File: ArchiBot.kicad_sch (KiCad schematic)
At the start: 0 parts

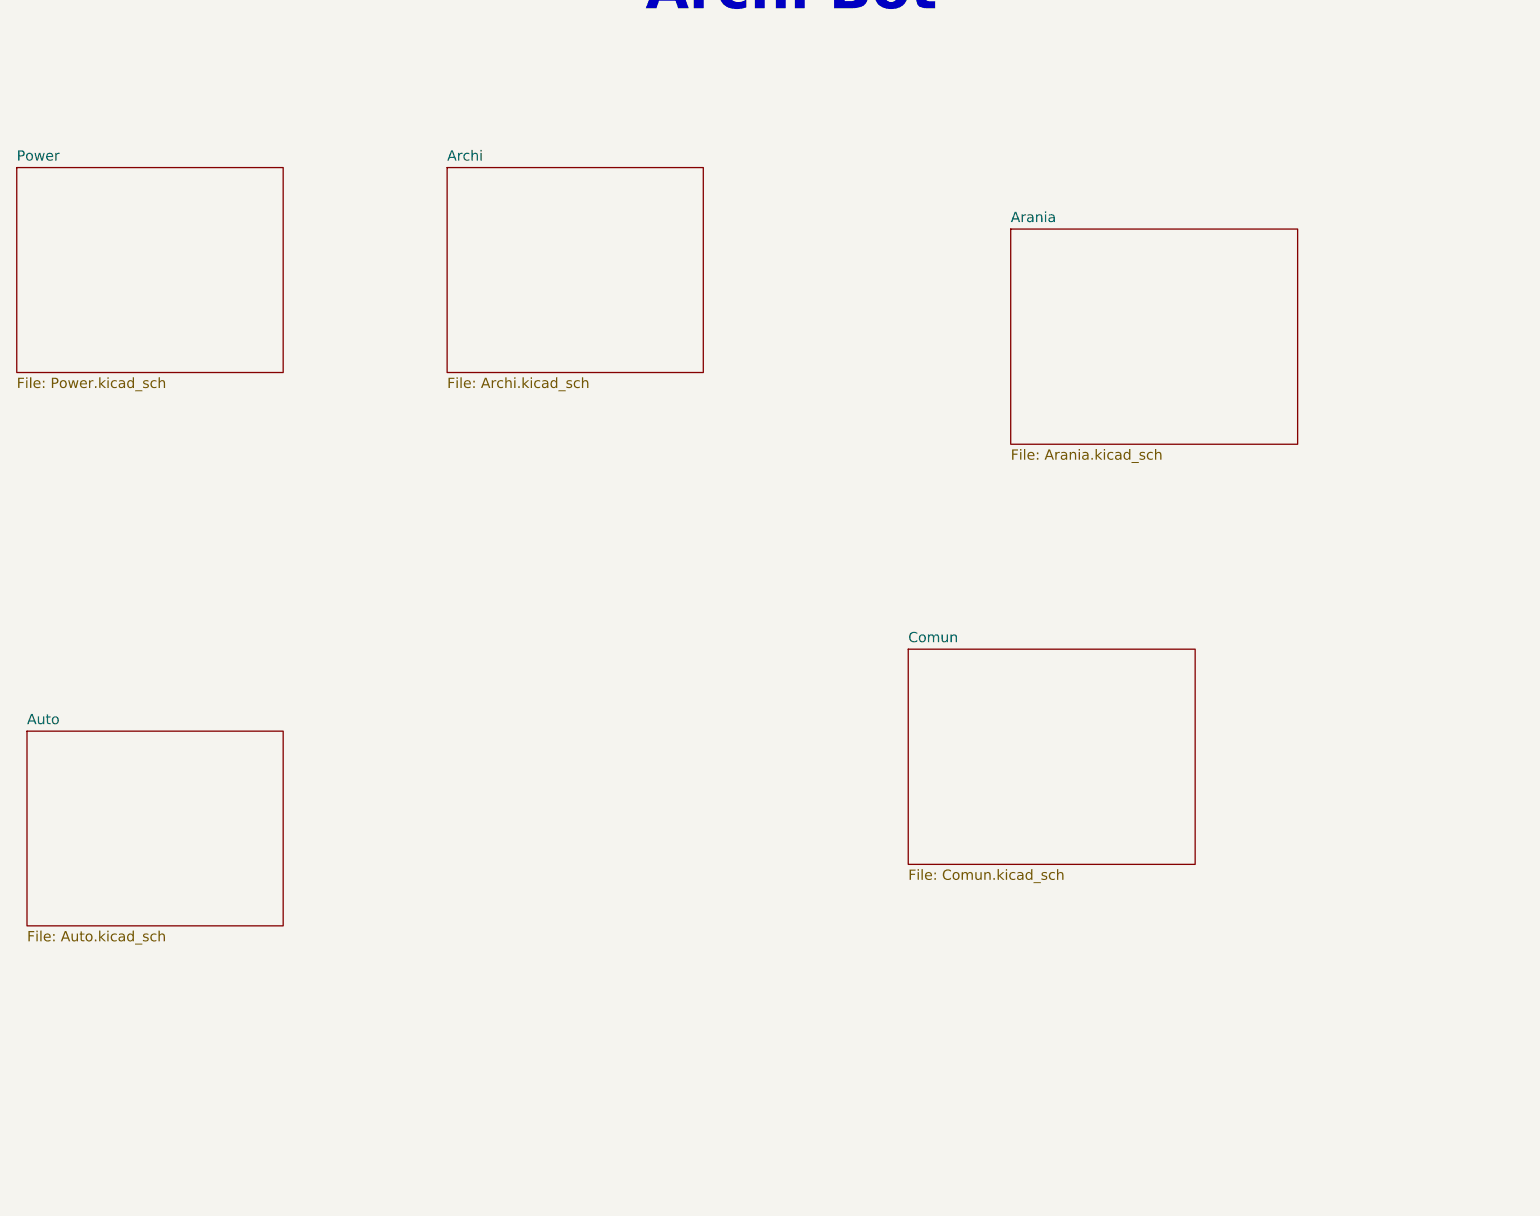
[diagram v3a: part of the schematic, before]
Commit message: Termino lista de materiales, ubico componentes e inicio ruteo
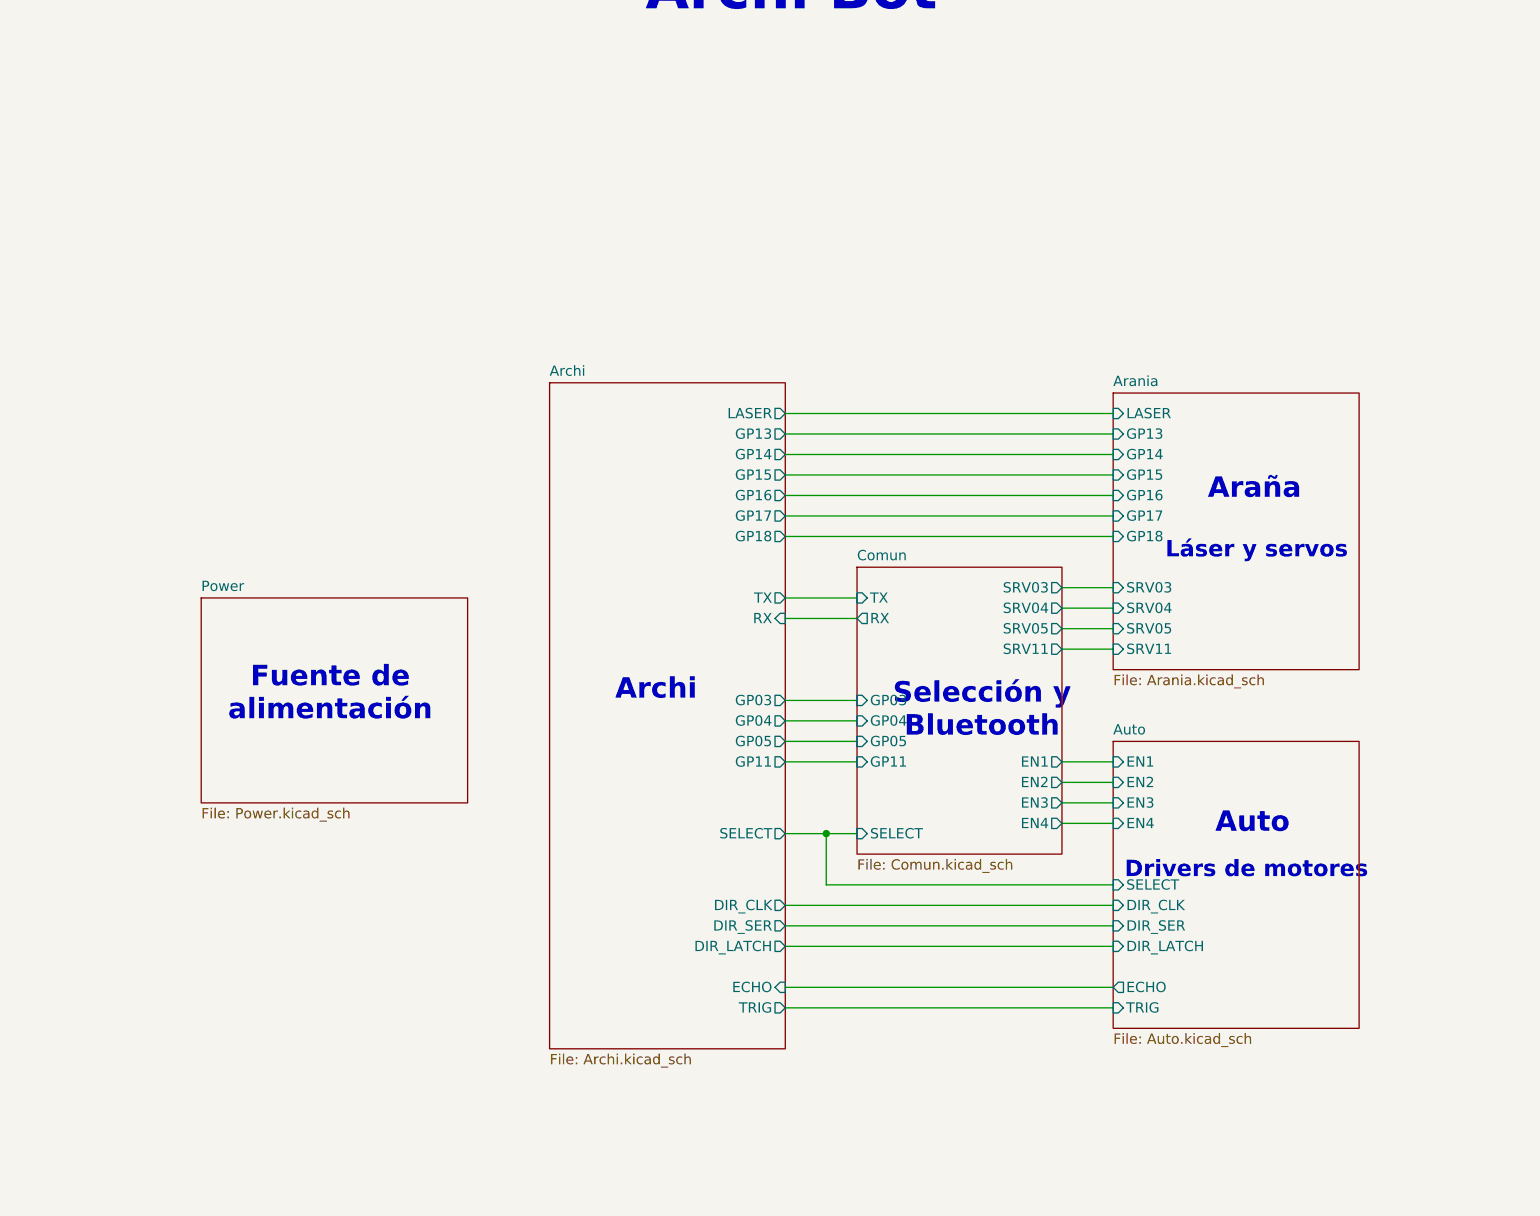
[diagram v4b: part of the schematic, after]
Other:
- sheet Arania ports: added GP13, GP14, GP15, GP16, GP17, GP18, LASER, SRV03, SRV04, SRV05, SRV11; removed none
- sheet Archi ports: added DIR_CLK, DIR_LATCH, DIR_SER, ECHO, GP03, GP04, GP05, GP11, GP13, GP14, GP15, GP16, GP17, GP18, LASER, RX, SELECT, TRIG, TX; removed none
- sheet Auto ports: added DIR_CLK, DIR_LATCH, DIR_SER, ECHO, EN1, EN2, EN3, EN4, SELECT, TRIG; removed none
- sheet Comun ports: added EN1, EN2, EN3, EN4, GP03, GP04, GP05, GP11, RX, SELECT, SRV03, SRV04, SRV05, SRV11, TX; removed none
- note added: "Araña"
- note added: "Archi"
- note added: "Auto"
- note added: "Drivers de motores"
- note added: "Fuente de alimentación"
- note added: "Láser y servos"
- note added: "Selección y Bluetooth"

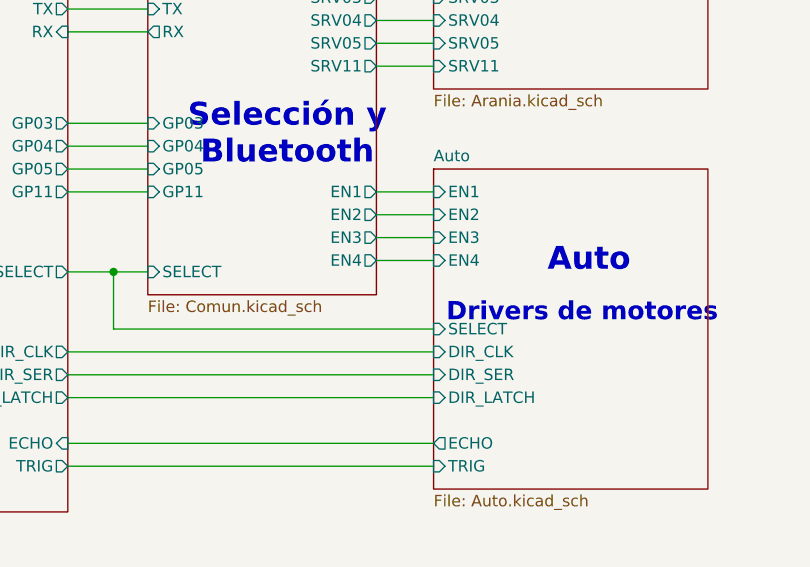
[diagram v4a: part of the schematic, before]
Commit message: Cambio componente principal, hago ubicación en PCB
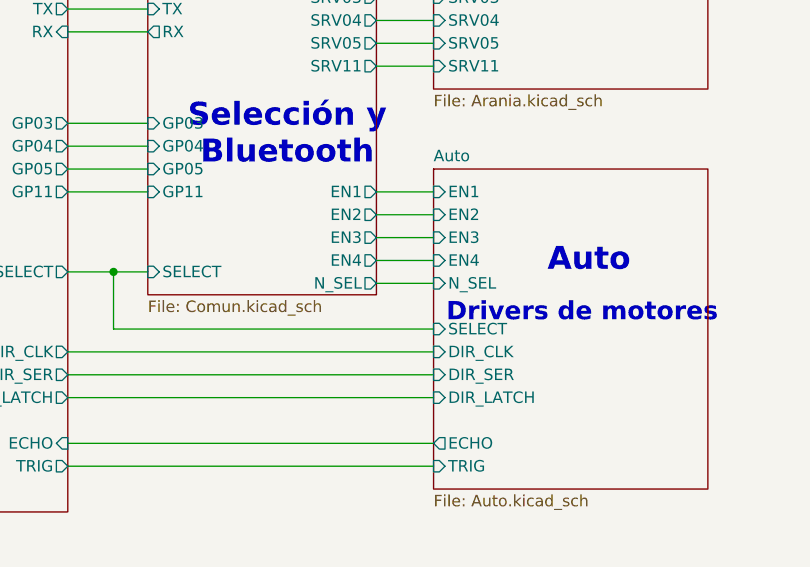
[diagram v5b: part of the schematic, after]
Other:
- sheet Auto ports: added N_SEL; removed none
- sheet Comun ports: added N_SEL; removed none
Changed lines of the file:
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@@
+	(wire
+		(pts
+			(xy 172.72 127) (xy 179.07 127)
+		)
+		(stroke
+			(width 0)
+			(type default)
+		)
+	)
 	(wire
 		(pts
@@
 			)
 		)
+		(pin "N_SEL" output
+			(at 172.72 127 0)
+			(effects
+				(font
+					(size 1.27 1.27)
+				)
+				(justify right)
+			)
+		)
 		(instances
 			(project "ArchiBot"
@@
 			(effects
 				(font
+					(size 1.27 1.27)
+				)
+				(justify left)
+			)
+		)
+		(pin "N_SEL" input
+			(at 179.07 127 180)
+			(effects
+				(font

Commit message: Finalizo ruteo version 1.1
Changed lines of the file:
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@@
 	(title_block
 		(title "Archi Bot")
-		(date "2024-06-24")
-		(rev "1.0")
+		(date "2024-07-18")
+		(rev "1.1")
 	)
 	(junction
